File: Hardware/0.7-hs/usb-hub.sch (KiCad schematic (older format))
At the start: 35 parts, among them J3 USB_C_Receptacle_USB2.0, J4 USB_C_Receptacle_USB2.0, J5 USB_C_Receptacle_USB2.0, U1 USBLC6-2SC6, U3 CY7C65632-28LTXCT, U4 USBLC6-2SC6, U5 USBLC6-2SC6, U6 USBLC6-2SC6, Y2 12MHz

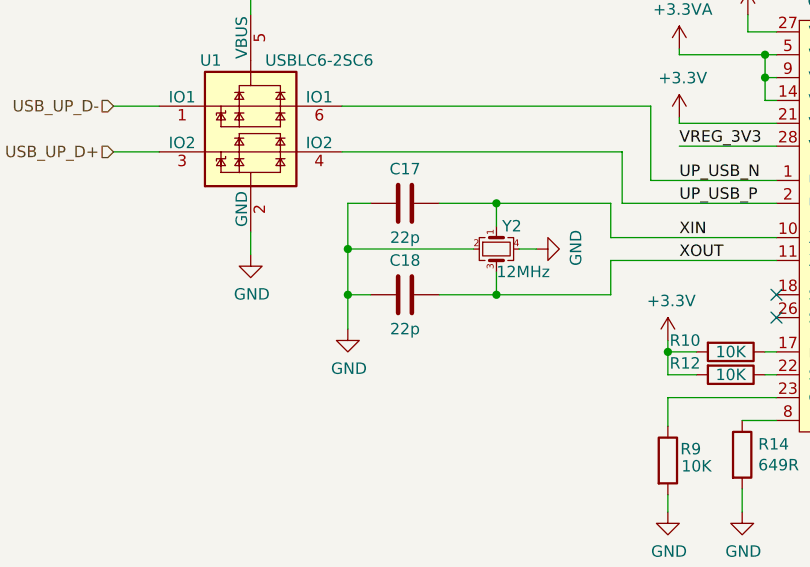
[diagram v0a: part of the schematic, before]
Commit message: update sockets with courtyard
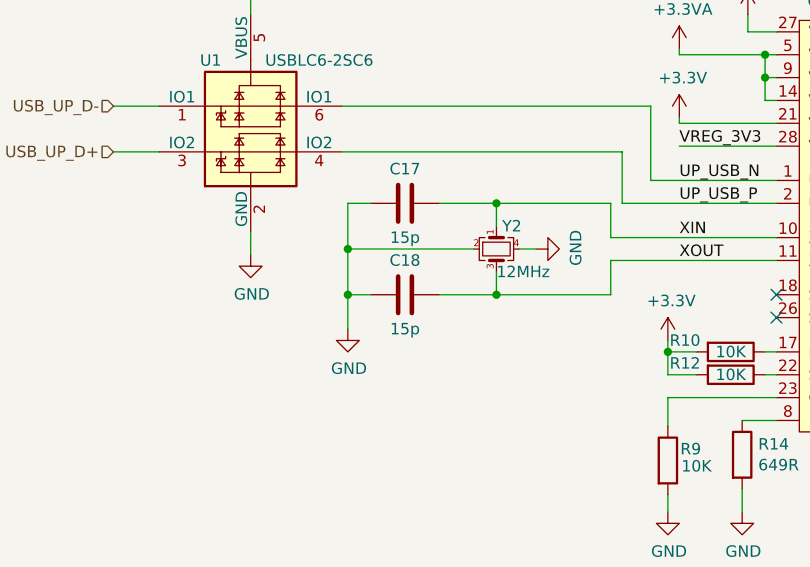
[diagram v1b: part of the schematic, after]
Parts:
- C12: DigiKey 1276-1000-1-ND -> 1276-1871-1-ND; LCSC C1591 -> C85713; MPN CL10B104KB8NNNC -> CL10A106MP8NNNC; Substitue Allowed? Y -> Y - X5R or better
- C13: DigiKey 1276-1871-1-ND -> 1276-1000-1-ND; LCSC C85713 -> C1591; MPN CL10A106MP8NNNC -> CL10B104KB8NNNC; Substitue Allowed? Y -> Y - X5R or better
- C14, C15, C16, C19, C20, C21, C22: Substitue Allowed? Y -> Y - X5R or better
- C17, C18: value 22p -> 15p; DigiKey 1276-2228-1-ND -> 1276-1296-2-ND; LCSC C1653 -> C1644; MPN CL10C220JB8NFNC -> CL10C150JB8NNNC; Substitue Allowed? Y -> Y - NP0 / C0G or better
- C24, C25, C26: DigiKey (none) -> 1276-1000-1-ND; LCSC (none) -> C1591; MPN (none) -> CL10B104KB8NNNC; Manufacturer (none) -> Samsung Electro-Mechanics; Substitue Allowed? (none) -> Y - X5R or better
- F2, F3, F4: DigiKey (none) -> 507-1811-1-ND; LCSC (none) -> C70057; MPN (none) -> 0ZCK0020FF2G; Manufacturer (none) -> Bel Fuse; Notes (none) -> LCSC: Substitute PN; Substitue Allowed? (none) -> Y - 200mA hold / 500mA trip
- FB1, FB2, FB3, FB4: DigiKey 490-1014-1-ND -> 490-5258-1-ND; LCSC C19330 -> C85833; MPN BLM18AG601SN1D -> BLM18KG601SN1D; Substitue Allowed? Y -> Y - 600R, > 1A current
- J3, J4, J5: Substitue Allowed? Y -> Y - Footprint / pinout compatiable
- R10, R12: DigiKey (none) -> CR0603-JW-103ELFCT-ND; LCSC (none) -> C144116; MPN (none) -> CR0603-JW-103ELF; Manufacturer (none) -> Bourns; Notes (none) -> LCSC: Substitute PN; Substitue Allowed? (none) -> Y - Same spec
- R14, RN5: Substitue Allowed? Y -> Y - Same spec
- R9: DigiKey CR0603-JW-104ELFCT-ND -> CR0603-JW-103ELFCT-ND; LCSC C203223 -> C144116; MPN CR0603-JW-104ELF -> CR0603-JW-103ELF; Substitue Allowed? Y -> Y - Same spec
- U1, U4, U5, U6: Manufacturer STmicroelectronics -> STMicroelectronics; Substitue Allowed? (none) -> N
- Y2: DigiKey 535-9826-1-ND -> 535-14962-6-ND; LCSC C276421 -> C164041; MPN ABM8-12.000MHZ-B2-T -> ABM8-12.000MHZ-12-B1U-T; Notes (none) -> LCSC: Substitute PN; Substitue Allowed? Y -> Y - 12 MHz, 10/12pF

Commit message: add note on uncommenting out code
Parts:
- C17, C18: Substitue Allowed? Y - NP0 / C0G or better -> Y - NP0 / C0G
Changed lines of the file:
@@
 F 4 "1276-1296-2-ND" H 2400 2375 50  0001 C CNN "DigiKey"
 F 5 "CL10C150JB8NNNC" H 2400 2375 50  0001 C CNN "MPN"
-F 6 "Y - NP0 / C0G or better" H 2400 2375 50  0001 C CNN "Substitue Allowed?"
+F 6 "Y - NP0 / C0G" H 2400 2375 50  0001 C CNN "Substitue Allowed?"
 F 7 "C1644" H 2400 2375 50  0001 C CNN "LCSC"
 F 8 "Samsung Electro-Mechanics" H 2400 2375 50  0001 C CNN "Manufacturer"
@@
 F 4 "1276-1296-2-ND" H 2400 1975 50  0001 C CNN "DigiKey"
 F 5 "CL10C150JB8NNNC" H 2400 1975 50  0001 C CNN "MPN"
-F 6 "Y - NP0 / C0G or better" H 2400 1975 50  0001 C CNN "Substitue Allowed?"
+F 6 "Y - NP0 / C0G" H 2400 1975 50  0001 C CNN "Substitue Allowed?"
 F 7 "C1644" H 2400 1975 50  0001 C CNN "LCSC"
 F 8 "Samsung Electro-Mechanics" H 2400 1975 50  0001 C CNN "Manufacturer"

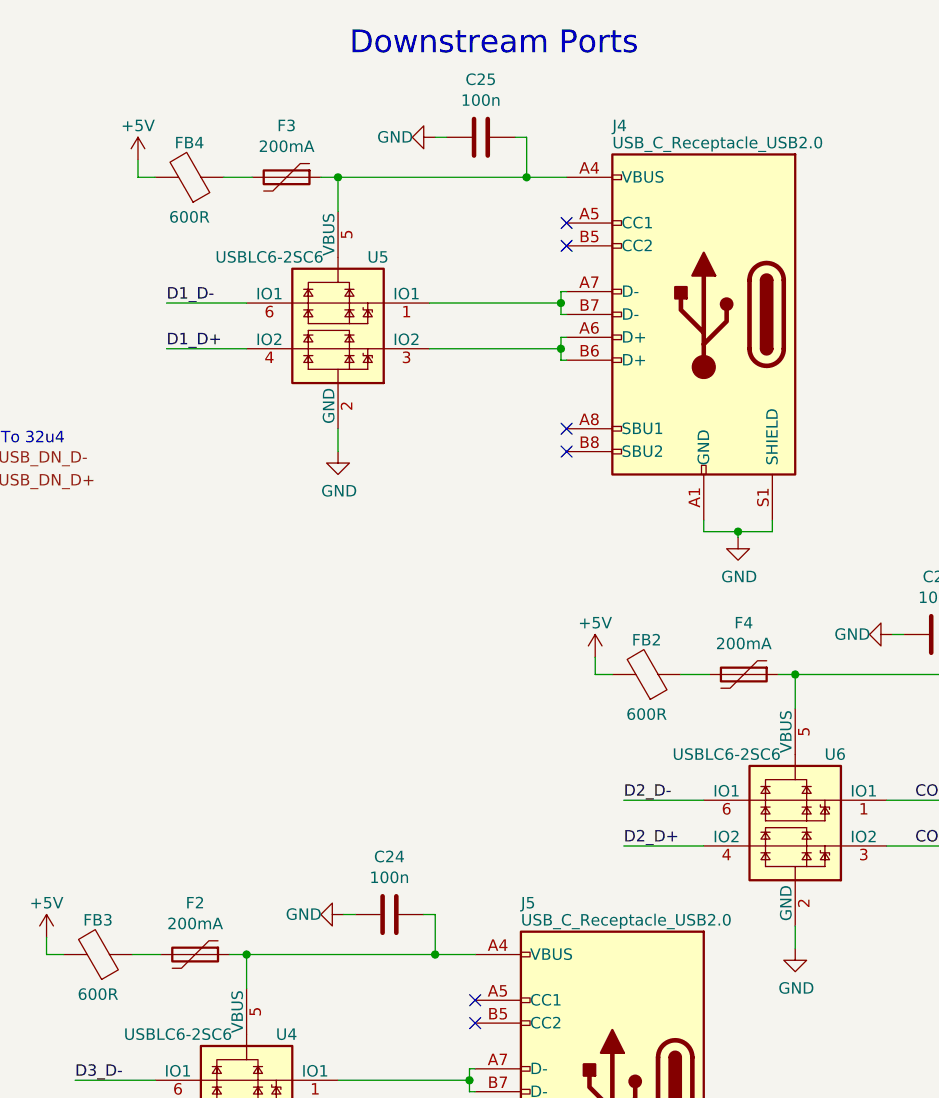
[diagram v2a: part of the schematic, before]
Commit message: update fuse values
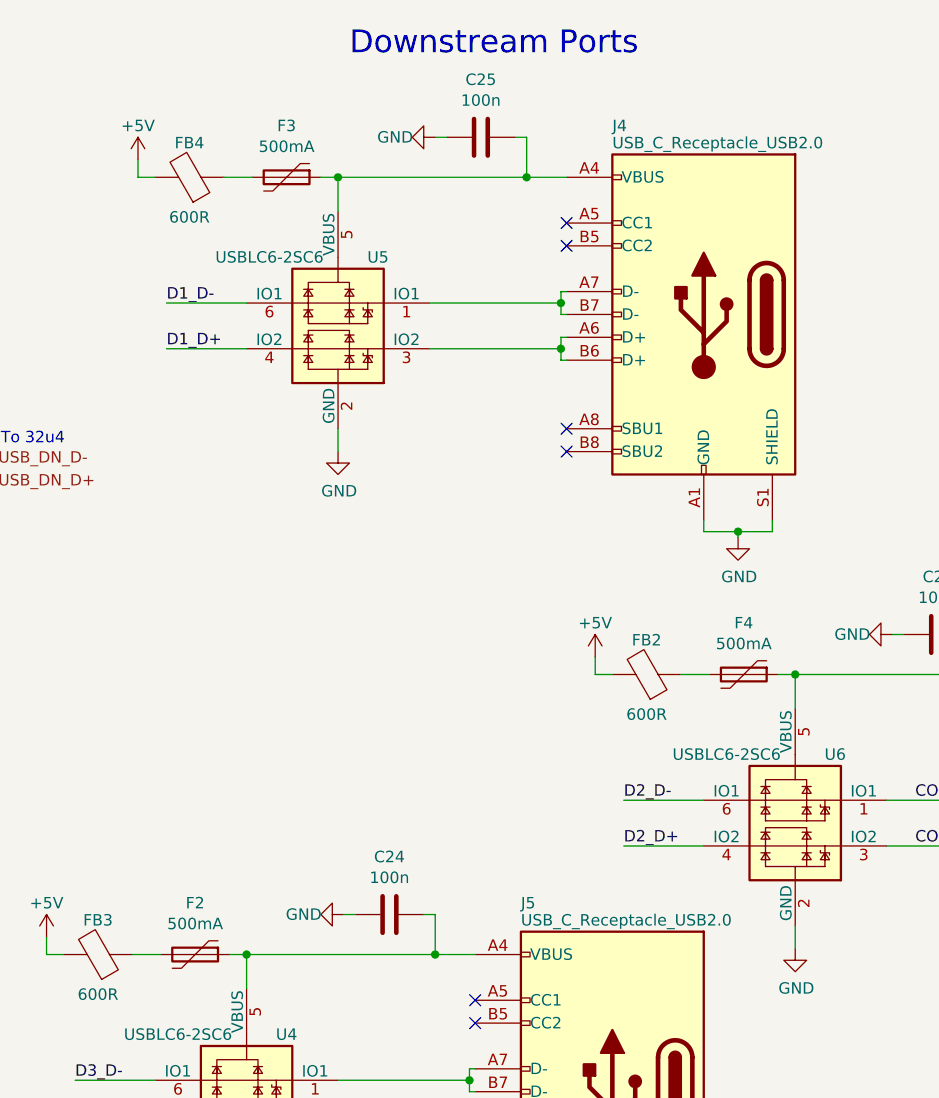
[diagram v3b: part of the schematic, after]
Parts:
- F2, F3, F4: value 200mA -> 500mA; DigiKey 507-1811-1-ND -> F2772CT-ND; LCSC C70057 -> C207022; MPN 0ZCK0020FF2G -> 0805L050WR; Manufacturer Bel Fuse -> Littelfuse; Notes LCSC: Substitute PN -> (none); Substitue Allowed? Y - 200mA hold / 500mA trip -> Y - 500mA hold / 1A trip
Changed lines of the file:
@@
 P 6700 1200
 F 0 "F3" V 6475 1200 50  0000 C CNN
-F 1 "200mA" V 6566 1200 50  0000 C CNN
+F 1 "500mA" V 6566 1200 50  0000 C CNN
 F 2 "josh-passives-smt:Fuse_0805_2012Metric" H 6750 1000 50  0001 L CNN
 F 3 "~" H 6700 1200 50  0001 C CNN
-F 4 "507-1811-1-ND" H 6700 1200 50  0001 C CNN "DigiKey"
-F 5 "C70057" H 6700 1200 50  0001 C CNN "LCSC"
-F 6 "0ZCK0020FF2G" H 6700 1200 50  0001 C CNN "MPN"
-F 7 "Bel Fuse" H 6700 1200 50  0001 C CNN "Manufacturer"
-F 8 "LCSC: Substitute PN" H 6700 1200 50  0001 C CNN "Notes"
-F 9 "Y - 200mA hold / 500mA trip" H 6700 1200 50  0001 C CNN "Substitue Allowed?"
+F 4 "F2772CT-ND" H 6700 1200 50  0001 C CNN "DigiKey"
+F 5 "C207022" H 6700 1200 50  0001 C CNN "LCSC"
+F 6 "0805L050WR" H 6700 1200 50  0001 C CNN "MPN"
+F 7 "Littelfuse" H 6700 1200 50  0001 C CNN "Manufacturer"
+F 8 "" H 6700 1200 50  0001 C CNN "Notes"
+F 9 "Y - 500mA hold / 1A trip" H 6700 1200 50  0001 C CNN "Substitue Allowed?"
 	1    6700 1200
 	0    1    1    0
@@
 P 8700 3375
 F 0 "F4" V 8475 3375 50  0000 C CNN
-F 1 "200mA" V 8566 3375 50  0000 C CNN
+F 1 "500mA" V 8566 3375 50  0000 C CNN
 F 2 "josh-passives-smt:Fuse_0805_2012Metric" H 8750 3175 50  0001 L CNN
 F 3 "~" H 8700 3375 50  0001 C CNN
-F 4 "507-1811-1-ND" H 8700 3375 50  0001 C CNN "DigiKey"
-F 5 "C70057" H 8700 3375 50  0001 C CNN "LCSC"
-F 6 "0ZCK0020FF2G" H 8700 3375 50  0001 C CNN "MPN"
-F 7 "Bel Fuse" H 8700 3375 50  0001 C CNN "Manufacturer"
-F 8 "LCSC: Substitute PN" H 8700 3375 50  0001 C CNN "Notes"
-F 9 "Y - 200mA hold / 500mA trip" H 8700 3375 50  0001 C CNN "Substitue Allowed?"
+F 4 "F2772CT-ND" H 8700 3375 50  0001 C CNN "DigiKey"
+F 5 "C207022" H 8700 3375 50  0001 C CNN "LCSC"
+F 6 "0805L050WR" H 8700 3375 50  0001 C CNN "MPN"
+F 7 "Littelfuse" H 8700 3375 50  0001 C CNN "Manufacturer"
+F 8 "" H 8700 3375 50  0001 C CNN "Notes"
+F 9 "Y - 500mA hold / 1A trip" H 8700 3375 50  0001 C CNN "Substitue Allowed?"
 	1    8700 3375
 	0    1    1    0
@@
 P 6300 4600
 F 0 "F2" V 6075 4600 50  0000 C CNN
-F 1 "200mA" V 6166 4600 50  0000 C CNN
+F 1 "500mA" V 6166 4600 50  0000 C CNN
 F 2 "josh-passives-smt:Fuse_0805_2012Metric" H 6350 4400 50  0001 L CNN
 F 3 "~" H 6300 4600 50  0001 C CNN
-F 4 "507-1811-1-ND" H 6300 4600 50  0001 C CNN "DigiKey"
-F 5 "C70057" H 6300 4600 50  0001 C CNN "LCSC"
-F 6 "0ZCK0020FF2G" H 6300 4600 50  0001 C CNN "MPN"
-F 7 "Bel Fuse" H 6300 4600 50  0001 C CNN "Manufacturer"
-F 8 "LCSC: Substitute PN" H 6300 4600 50  0001 C CNN "Notes"
-F 9 "Y - 200mA hold / 500mA trip" H 6300 4600 50  0001 C CNN "Substitue Allowed?"
+F 4 "F2772CT-ND" H 6300 4600 50  0001 C CNN "DigiKey"
+F 5 "C207022" H 6300 4600 50  0001 C CNN "LCSC"
+F 6 "0805L050WR" H 6300 4600 50  0001 C CNN "MPN"
+F 7 "Littelfuse" H 6300 4600 50  0001 C CNN "Manufacturer"
+F 8 "" H 6300 4600 50  0001 C CNN "Notes"
+F 9 "Y - 500mA hold / 1A trip" H 6300 4600 50  0001 C CNN "Substitue Allowed?"
 	1    6300 4600
 	0    1    1    0
